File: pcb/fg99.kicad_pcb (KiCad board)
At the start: 2 copper layers, 100.1 x 63.1 mm, 34 parts, among them M1 SD_Module, M2 SD_Slot, P1 CONN_02X18, P3 CONN_02X03, SW1 SW_PUSH, SW2 SW_PUSH, U1 XC95144XL-TQ100, U2 CY62158E-TSOP44, U3 ATMEGA328P-TQFP32, U4 NCP1117

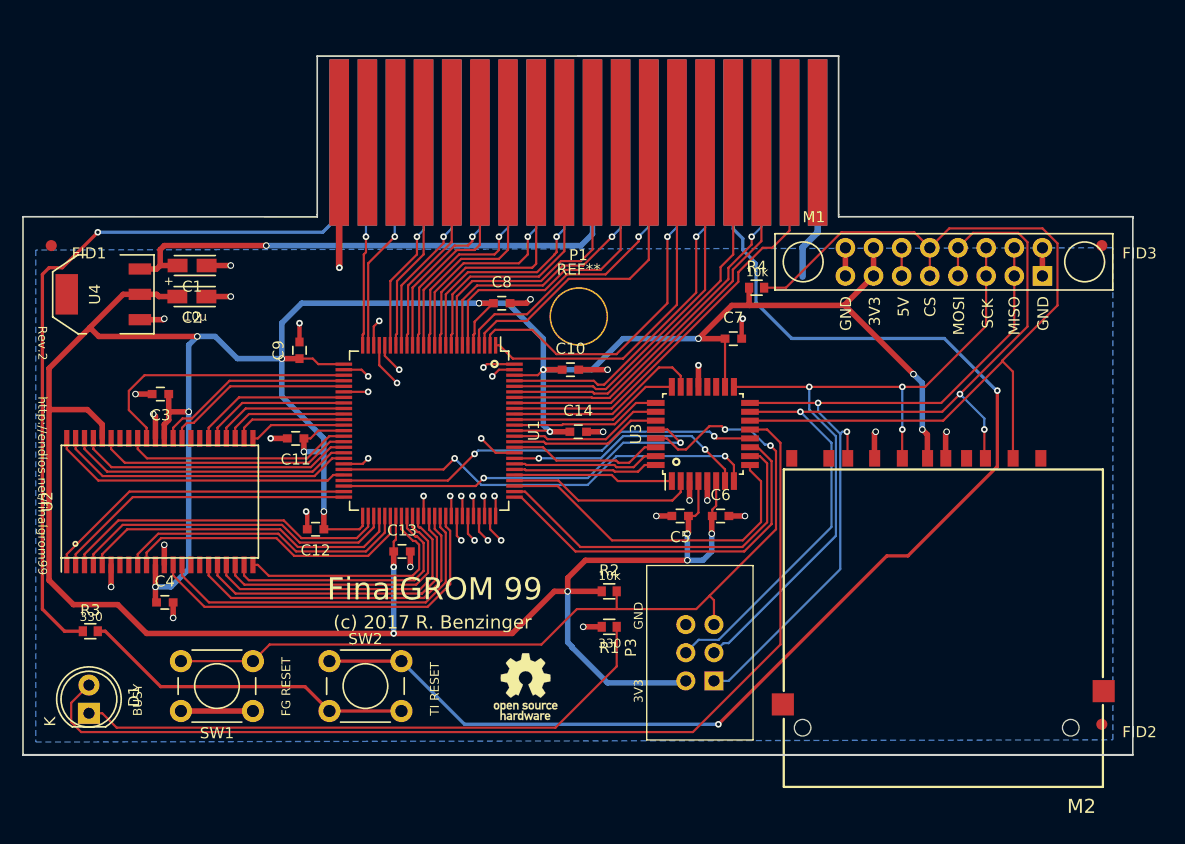
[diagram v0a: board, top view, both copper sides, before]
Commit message: Increase via sizes and add shorting bar for hard gold plating on the card edge
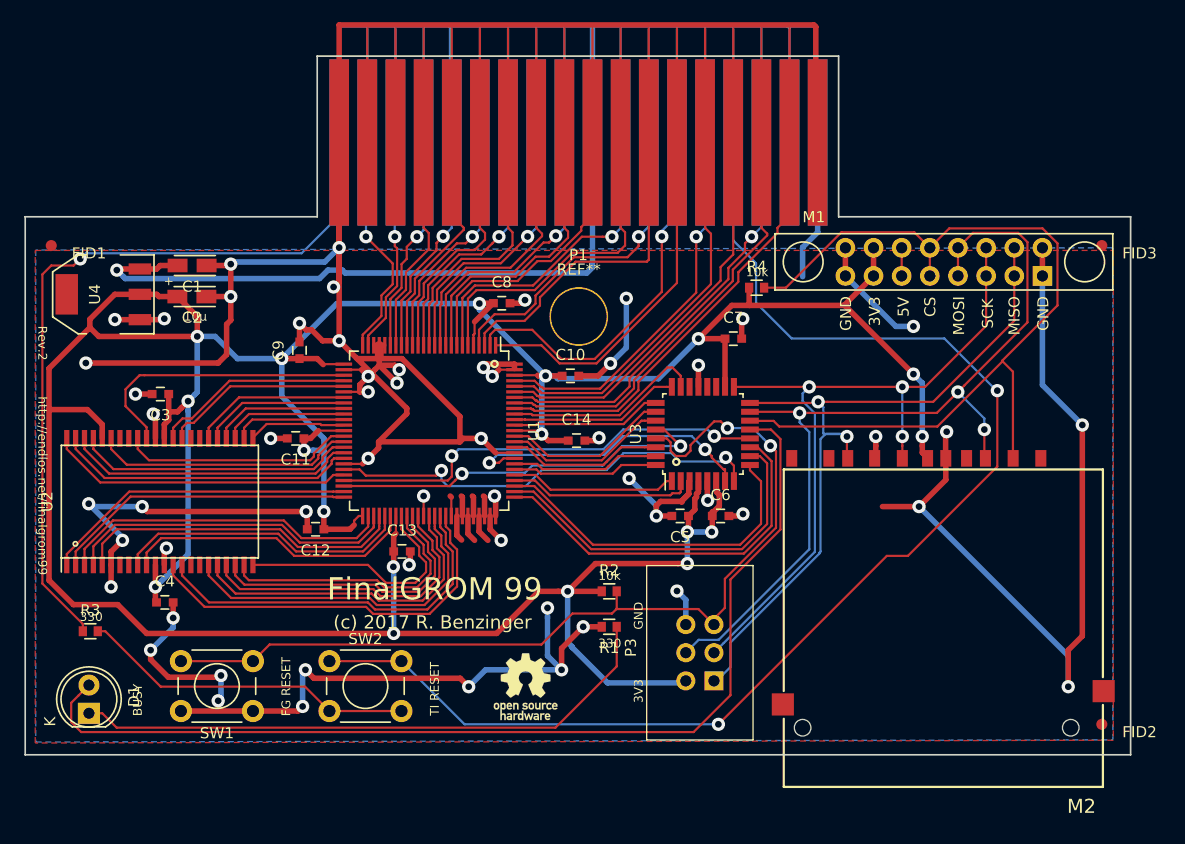
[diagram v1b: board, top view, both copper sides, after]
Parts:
- moved C14 0.81 mm to (143.4, 67.1)
- moved C10 0.56 mm to (142.8, 61.2)
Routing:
- net GND: track 121.2 -> 467.8 mm, vias 42 -> 57
- net /TIRS: track 70.3 -> 153.6 mm
- net +5V: track 52.8 -> 71.1 mm
- net (no net): track 4.78 -> 20.5 mm, vias 2 -> 0
- net /BD0: track 18.5 -> 30.7 mm
- net /WE*: track 37.8 -> 49.2 mm
- net /BA2: track 20.0 -> 31.1 mm
- net /GR: track 37.3 -> 48.3 mm
- net /BA10: track 34.3 -> 45.3 mm
- net /BA1: track 28.4 -> 39.4 mm
- net /BA8: track 29.4 -> 40.1 mm
- net /BA12: track 29.2 -> 39.9 mm
- net /BA0: track 19.3 -> 30.0 mm
- net /BA3: track 21.5 -> 32.2 mm
- net /BA4: track 23.2 -> 33.8 mm
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- added copper zone on F.Cu, net GND
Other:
- board size 100.1 x 63.1 mm -> 99.8 x 63.1 mm
- net class Default: via_dia 0.6 -> 1.2; via_drill 0.3 -> 0.6
- net class Pconn: via_dia 0.6 -> 1.2; via_drill 0.3 -> 0.6
- net class Power: via_dia 0.6 -> 1.2; via_drill 0.4 -> 0.6

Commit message: Clean up silk
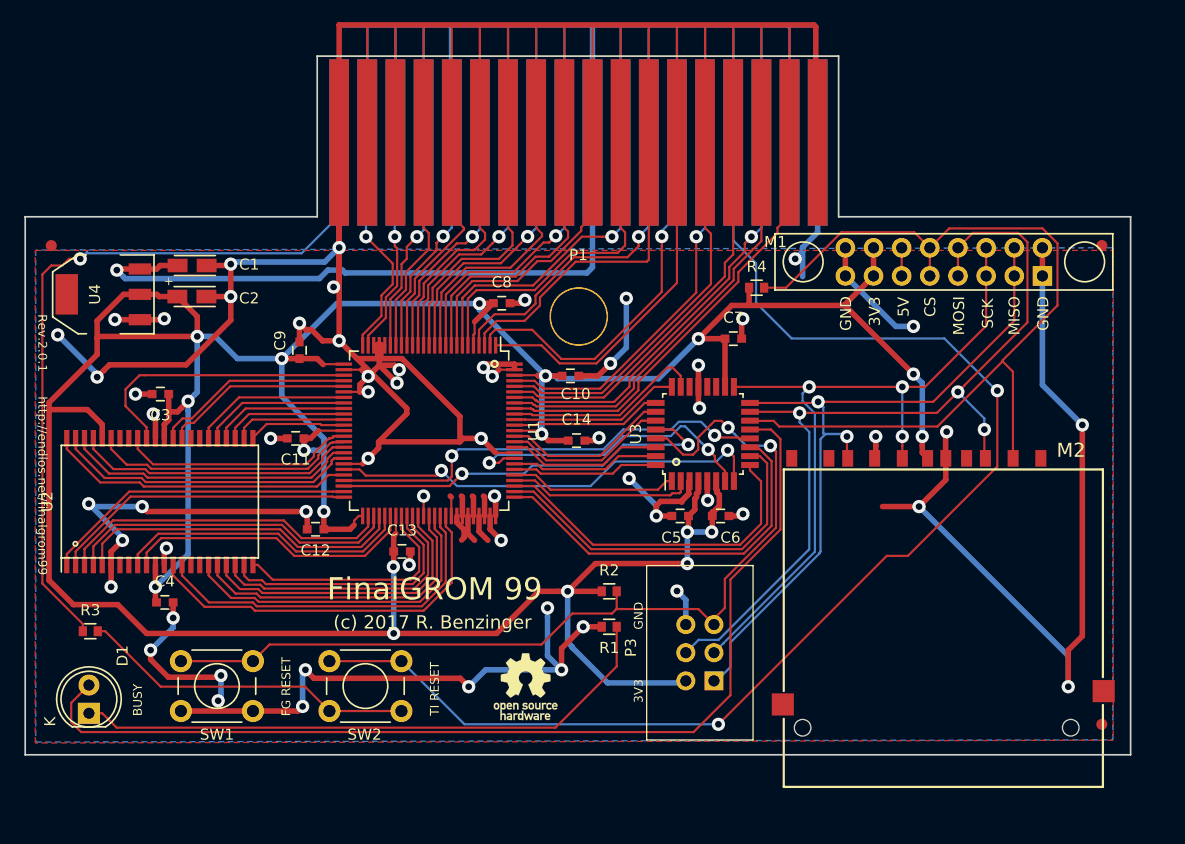
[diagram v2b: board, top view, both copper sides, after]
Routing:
- net GND: track 467.8 -> 474.5 mm, vias 57 -> 60
- net +3V3: track 350.2 -> 348.8 mm
- net /TCK: track 34.7 -> 36.1 mm
- net /RD3: track 34.2 -> 33.0 mm
- net /RA17: track 26.4 -> 25.3 mm
- net /RA19: track 29.4 -> 28.2 mm
- net /RA15: track 22.7 -> 21.5 mm
- net /RA16: track 24.8 -> 23.7 mm
- net /RWE*: track 31.0 -> 29.8 mm
- net /RA18: track 28.0 -> 26.8 mm
- net /RD2: track 35.8 -> 34.7 mm
- net /TDO: track 27.1 -> 27.9 mm
- net /TMS: track 40.0 -> 40.6 mm
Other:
- board text added: "Rev.2.0.1"
- board text removed: "Rev.2"
